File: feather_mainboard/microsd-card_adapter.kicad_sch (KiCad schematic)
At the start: 12 parts, among them J4 693071020811, J5 61300211121, J7 61300211121, J8 61300211121

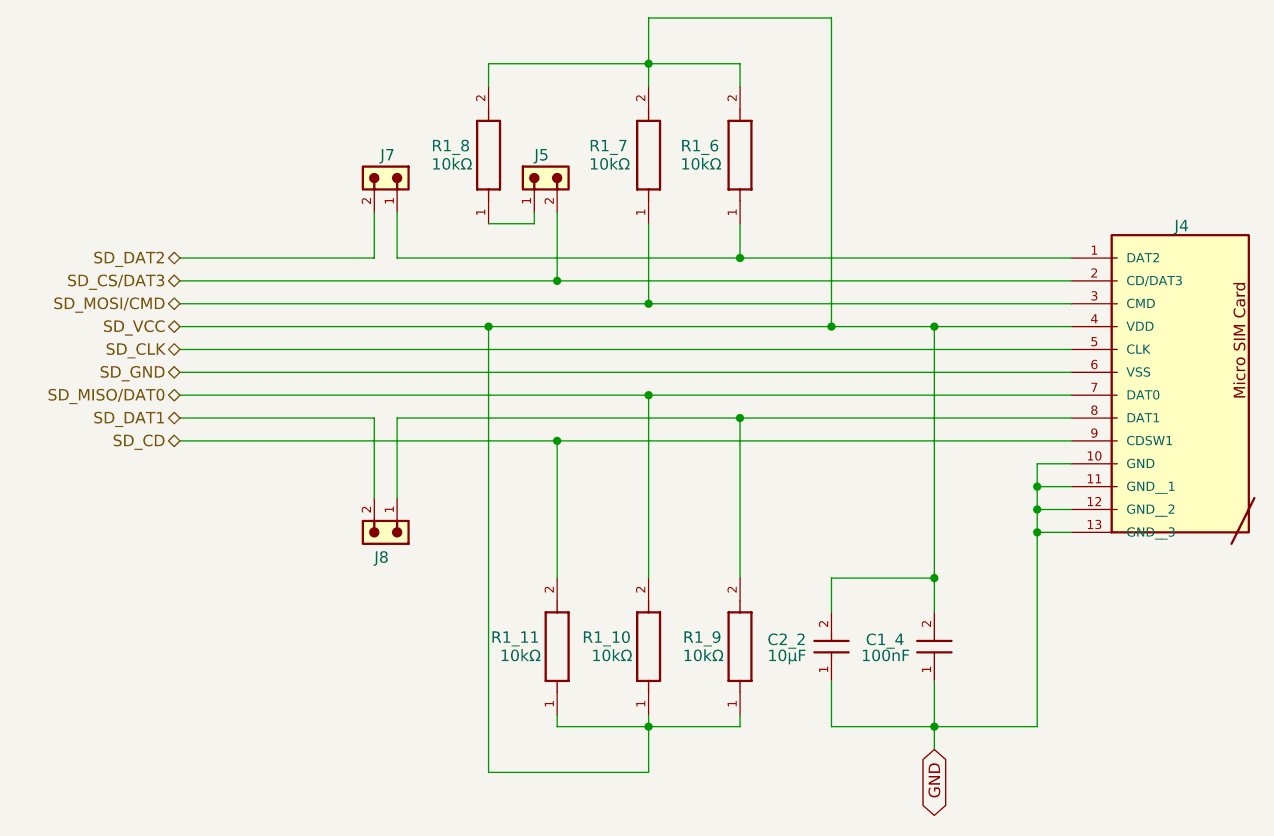
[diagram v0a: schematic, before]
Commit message: Updated the mainboard: removed unnecessary pull-ups on SD card lines; connected IIC pull-ups to enable circuit; cleaned up schematic
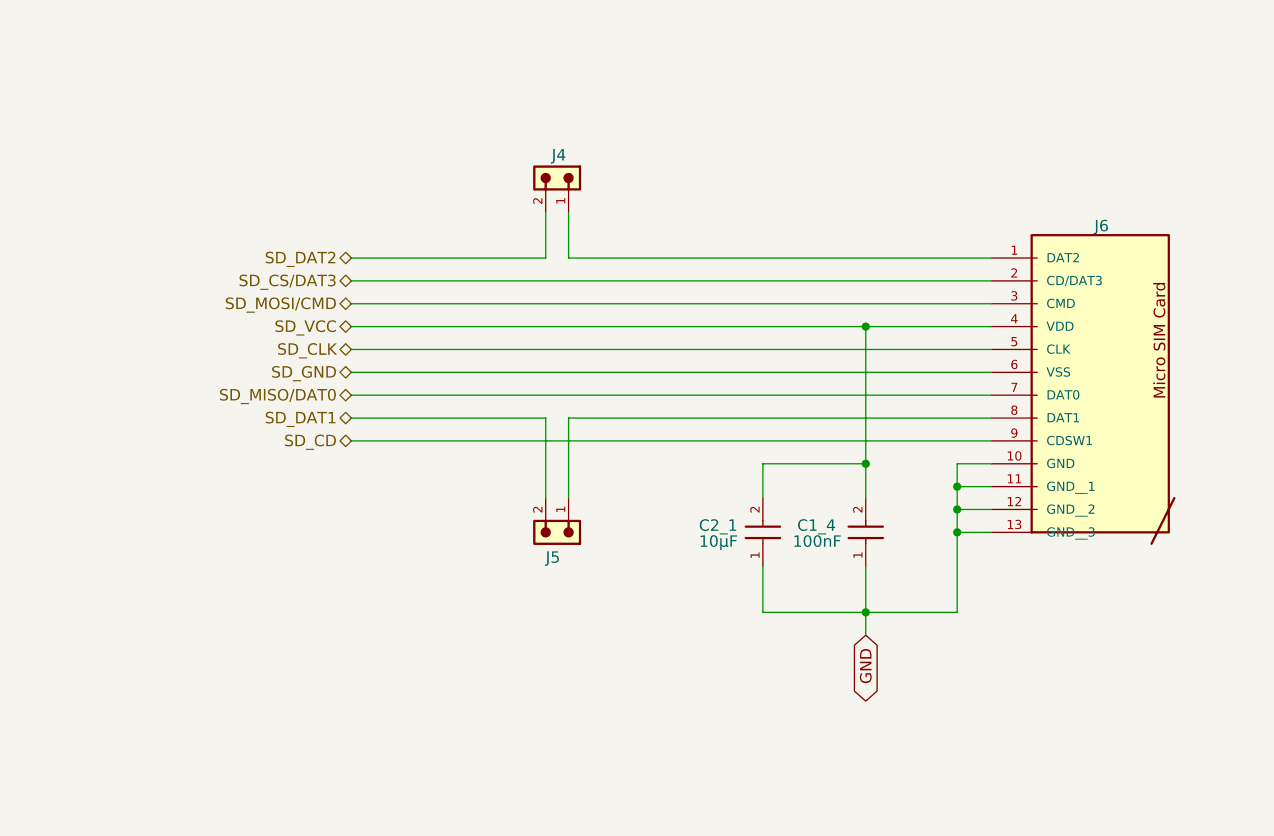
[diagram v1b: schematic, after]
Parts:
- removed J5: 61300211121, Custom footprints:61300211121, symbol 6130XX11121_61300211121:6130XX11121_61300211121
- removed R1_10, R1_11, R1_6, R1_7, R1_8, R1_9: 10kΩ, Custom footprints:WRIS-RSKS_0603_REFLOW, symbol WRIS-RSKS_0603:WRIS-RSKS_0603
- renumbered C2_2 to C2_1, J7 to J4, J8 to J5, J4 to J6
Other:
- moved on the sheet: C1_4, C2_1, J4, J5, J6
